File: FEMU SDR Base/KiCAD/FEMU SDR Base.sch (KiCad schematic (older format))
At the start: 93 parts, among them M1 M1, M10 M1, M11 M1, M12 M1, M13 M1, M14 M1, M15 M1, M16 M1, M17 SMA1, M18 SMA2, M2 M1, M3 M1, M4 M1, M5 M1, M6 M1, M7 M1, M8 M1, M9 M1, P1 Battery, P10 PWM2, P11 PWM3, P12 PWM4, P13 PWM1, P14 PWM2, P15 PWM3, P16 PWM4, P17 12V, P18 GND, P19 12V, P2 SDR_Shield_1, P20 GND, P21 SDR0, P22 SDR1, P27 PWM0, P28 PWM5, P29 PWM6, P3 SDR_Shield_2, P30 PWM7, P31 PWM0, P32 PWM5, P33 PWM6, P34 PWM7, P35 Battery, P36 RPi, P37 PXH, P38 Rx, P4 12V, P5 GND, P6 12V, P7 GND, P8 Raspi_Power_Shield, P9 PWM1, U1 TPS562209, U2 LP38858-LDO, U3 LP38858-LDO, U4 LM1117, U5 LM1117

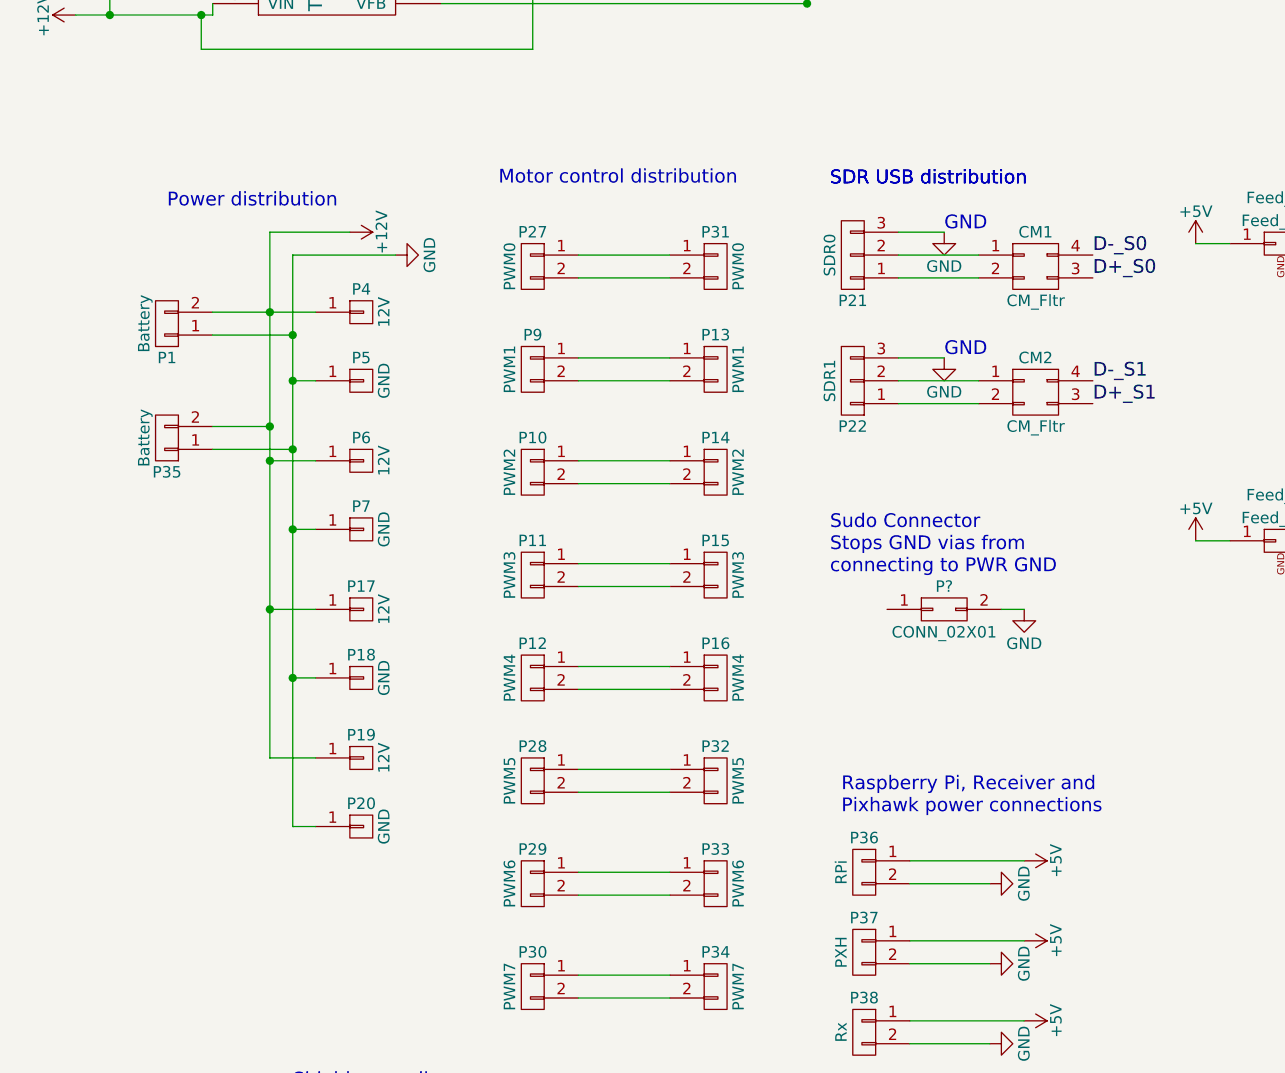
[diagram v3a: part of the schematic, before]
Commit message: Disconnected VIA connections from GND (layer2) onto PWR_GND current zones for motor return. Added sudo pads in Schematic to allow the GND and PWR_GND nets to connect
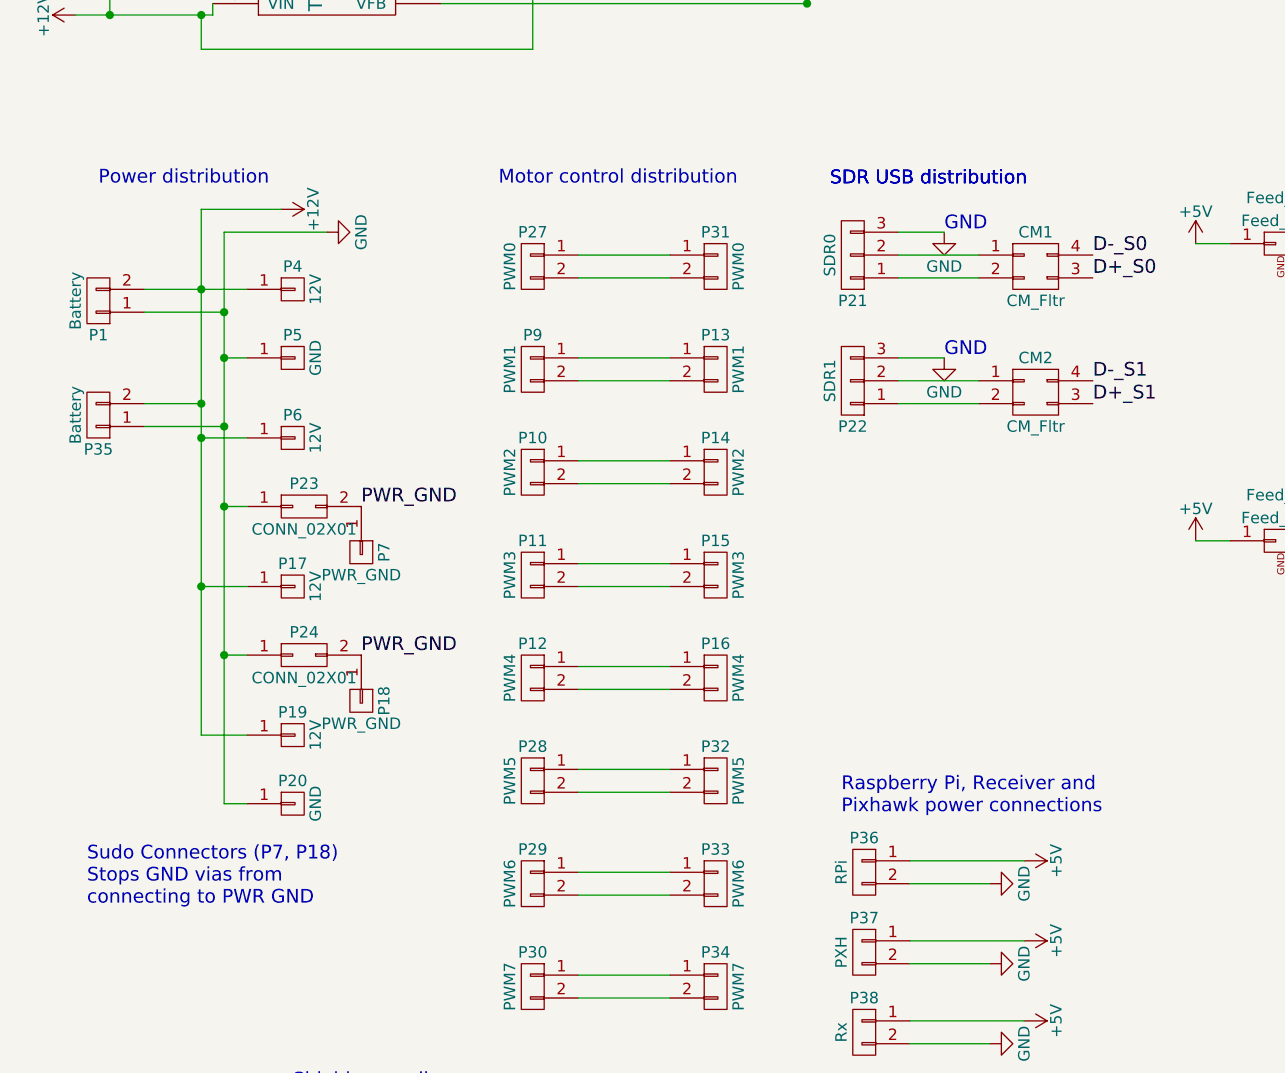
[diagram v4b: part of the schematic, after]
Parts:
- added P24: CONN_02X01, ARB_foots:Conn_PWR_GND_to_GND, symbol CONN_02X01
- C23: footprint Capacitors_SMD:C_0805_HandSoldering -> Capacitors_SMD:C_0603_HandSoldering
- P18, P7: value GND -> PWR_GND
- P23: renamed from P?; footprint (none) -> ARB_foots:Conn_PWR_GND_to_GND
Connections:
- net GND: now also P23.1 (P1), P24.1 (P1); no longer P18.1 (P1), P23.2 (P2), P7.1 (P1)
- new net PWR_GND: P18.1 (P1), P23.2 (P2), P24.2 (P2), P7.1 (P1)
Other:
- note added: "Sudo Connectors (P7, P18)\nStops GND vias from \nconnecting to PWR GND"
- note removed: "Sudo Connector\nStops GND vias from \nconnecting to PWR GND"
- moved on the sheet: P1, P17, P18, P19, P20, P23, P35, P4, P5, P6, P7
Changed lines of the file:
@@
 L CONN_01X02 P1
 U 1 1 572239A5
-P 1100 2950
-F 0 "P1" H 1100 3100 50  0000 C CNN
-F 1 "Battery" V 1200 2950 50  0000 C CNN
-F 2 "Misc footprints:XT60" H 1100 2950 50  0001 C CNN
-F 3 "" H 1100 2950 50  0000 C CNN
-	1    1100 2950
+P 800 2850
+F 0 "P1" H 800 3000 50  0000 C CNN
+F 1 "Battery" V 900 2850 50  0000 C CNN
+F 2 "Misc footprints:XT60" H 800 2850 50  0001 C CNN
+F 3 "" H 800 2850 50  0000 C CNN
+	1    800  2850
 	-1   0    0    1
 $EndComp
@@
 L +12V #PWR03
 U 1 1 5722422D
-P 1900 2550
-F 0 "#PWR03" H 1900 2400 50  0001 C CNN
-F 1 "+12V" H 1900 2690 50  0000 C CNN
-F 2 "" H 1900 2550 50  0000 C CNN
-F 3 "" H 1900 2550 50  0000 C CNN
-	1    1900 2550
+P 1600 2450
+F 0 "#PWR03" H 1600 2300 50  0001 C CNN
+F 1 "+12V" H 1600 2590 50  0000 C CNN
+F 2 "" H 1600 2450 50  0000 C CNN
+F 3 "" H 1600 2450 50  0000 C CNN
+	1    1600 2450
 	0    1    1    0
 $EndComp
-Text Notes 1100 2450 0    60   ~ 0
+Text Notes 800  2350 0    60   ~ 0
 Power distribution\n
 $Comp
@@
 L CONN_01X01 P4
 U 1 1 57343B65
-P 1950 2900
-F 0 "P4" H 1950 3000 50  0000 C CNN
-F 1 "12V" V 2050 2900 50  0000 C CNN
-F 2 "SMD_Packages:1Pin" H 1950 2900 50  0001 C CNN
-F 3 "" H 1950 2900 50  0000 C CNN
-	1    1950 2900
+P 1650 2800
+F 0 "P4" H 1650 2900 50  0000 C CNN
+F 1 "12V" V 1750 2800 50  0000 C CNN
+F 2 "SMD_Packages:1Pin" H 1650 2800 50  0001 C CNN
+F 3 "" H 1650 2800 50  0000 C CNN
+	1    1650 2800
 	1    0    0    -1
 $EndComp
@@
 L CONN_01X01 P5
 U 1 1 57343E6C
-P 1950 3200
-F 0 "P5" H 1950 3300 50  0000 C CNN
-F 1 "GND" V 2050 3200 50  0000 C CNN
-F 2 "SMD_Packages:1Pin" H 1950 3200 50  0001 C CNN
-F 3 "" H 1950 3200 50  0000 C CNN
-	1    1950 3200
+P 1650 3100
+F 0 "P5" H 1650 3200 50  0000 C CNN
+F 1 "GND" V 1750 3100 50  0000 C CNN
+F 2 "SMD_Packages:1Pin" H 1650 3100 50  0001 C CNN
+F 3 "" H 1650 3100 50  0000 C CNN
+	1    1650 3100
 	1    0    0    -1
 $EndComp
@@
 L CONN_01X01 P6
 U 1 1 57344192
-P 1950 3550
-F 0 "P6" H 1950 3650 50  0000 C CNN
-F 1 "12V" V 2050 3550 50  0000 C CNN
-F 2 "SMD_Packages:1Pin" H 1950 3550 50  0001 C CNN
-F 3 "" H 1950 3550 50  0000 C CNN
-	1    1950 3550
+P 1650 3450
+F 0 "P6" H 1650 3550 50  0000 C CNN
+F 1 "12V" V 1750 3450 50  0000 C CNN
+F 2 "SMD_Packages:1Pin" H 1650 3450 50  0001 C CNN
+F 3 "" H 1650 3450 50  0000 C CNN
+	1    1650 3450
 	1    0    0    -1
 $EndComp
@@
 L CONN_01X01 P7
 U 1 1 57344242
-P 1950 3850
-F 0 "P7" H 1950 3950 50  0000 C CNN
-F 1 "GND" V 2050 3850 50  0000 C CNN
-F 2 "SMD_Packages:1Pin" H 1950 3850 50  0001 C CNN
-F 3 "" H 1950 3850 50  0000 C CNN
-	1    1950 3850
-	1    0    0    -1
+P 1950 3950
+F 0 "P7" H 1950 4050 50  0000 C CNN
+F 1 "PWR_GND" V 2050 3950 50  0000 C CNN
+F 2 "SMD_Packages:1Pin" H 1950 3950 50  0001 C CNN
+F 3 "" H 1950 3950 50  0000 C CNN
+	1    1950 3950
+	0    1    1    0
 $EndComp
 $Comp
 L CONN_01X01 P17
 U 1 1 57345117
-P 1950 4200
-F 0 "P17" H 1950 4300 50  0000 C CNN
-F 1 "12V" V 2050 4200 50  0000 C CNN
-F 2 "SMD_Packages:1Pin" H 1950 4200 50  0001 C CNN
-F 3 "" H 1950 4200 50  0000 C CNN
-	1    1950 4200
+P 1650 4100
+F 0 "P17" H 1650 4200 50  0000 C CNN
+F 1 "12V" V 1750 4100 50  0000 C CNN
+F 2 "SMD_Packages:1Pin" H 1650 4100 50  0001 C CNN
+F 3 "" H 1650 4100 50  0000 C CNN
+	1    1650 4100
 	1    0    0    -1
 $EndComp
@@
 L CONN_01X01 P18
 U 1 1 5734511D
-P 1950 4500
-F 0 "P18" H 1950 4600 50  0000 C CNN
-F 1 "GND" V 2050 4500 50  0000 C CNN
-F 2 "SMD_Packages:1Pin" H 1950 4500 50  0001 C CNN
-F 3 "" H 1950 4500 50  0000 C CNN
-	1    1950 4500
-	1    0    0    -1
+P 1950 4600
+F 0 "P18" H 1950 4700 50  0000 C CNN
+F 1 "PWR_GND" V 2050 4600 50  0000 C CNN
+F 2 "SMD_Packages:1Pin" H 1950 4600 50  0001 C CNN
+F 3 "" H 1950 4600 50  0000 C CNN
+	1    1950 4600
+	0    1    1    0
 $EndComp
 $Comp
 L CONN_01X01 P19
 U 1 1 5734526F
-P 1950 4850
-F 0 "P19" H 1950 4950 50  0000 C CNN
-F 1 "12V" V 2050 4850 50  0000 C CNN
-F 2 "SMD_Packages:1Pin" H 1950 4850 50  0001 C CNN
-F 3 "" H 1950 4850 50  0000 C CNN
-	1    1950 4850
+P 1650 4750
+F 0 "P19" H 1650 4850 50  0000 C CNN
+F 1 "12V" V 1750 4750 50  0000 C CNN
+F 2 "SMD_Packages:1Pin" H 1650 4750 50  0001 C CNN
+F 3 "" H 1650 4750 50  0000 C CNN
+	1    1650 4750
 	1    0    0    -1
 $EndComp
@@
 L CONN_01X01 P20
 U 1 1 57345275
-P 1950 5150
-F 0 "P20" H 1950 5250 50  0000 C CNN
-F 1 "GND" V 2050 5150 50  0000 C CNN
-F 2 "SMD_Packages:1Pin" H 1950 5150 50  0001 C CNN
-F 3 "" H 1950 5150 50  0000 C CNN
-	1    1950 5150
+P 1650 5050
+F 0 "P20" H 1650 5150 50  0000 C CNN
+F 1 "GND" V 1750 5050 50  0000 C CNN
+F 2 "SMD_Packages:1Pin" H 1650 5050 50  0001 C CNN
+F 3 "" H 1650 5050 50  0000 C CNN
+	1    1650 5050
 	1    0    0    -1
 $EndComp
@@
 L GND #PWR015
 U 1 1 5734BB86
-P 2100 2650
-F 0 "#PWR015" H 2100 2400 50  0001 C CNN
-F 1 "GND" H 2100 2500 50  0000 C CNN
-F 2 "" H 2100 2650 50  0000 C CNN
-F 3 "" H 2100 2650 50  0000 C CNN
-	1    2100 2650
+P 1800 2550
+F 0 "#PWR015" H 1800 2300 50  0001 C CNN
+F 1 "GND" H 1800 2400 50  0000 C CNN
+F 2 "" H 1800 2550 50  0000 C CNN
+F 3 "" H 1800 2550 50  0000 C CNN
+	1    1800 2550
 	0    -1   -1   0
 $EndComp
@@
 F 0 "C23" H 8475 4550 50  0000 L CNN
 F 1 "10uF" H 8475 4350 50  0000 L CNN
-F 2 "Capacitors_SMD:C_0805_HandSoldering" H 8488 4300 50  0001 C CNN
+F 2 "Capacitors_SMD:C_0603_HandSoldering" H 8488 4300 50  0001 C CNN
 F 3 "" H 8450 4450 50  0000 C CNN
 	1    8450 4450
@@
 	3350 1100 3150 1100
 Wire Wire Line
-	1550 2550 1900 2550
+	1250 2450 1600 2450
 Wire Wire Line
 	2900 3100 3300 3100
@@
 	10350 4250 10350 4100
 Wire Wire Line
-	1300 2900 1750 2900
-Wire Wire Line
-	1550 2550 1550 4850
-Connection ~ 1550 2900
-Wire Wire Line
-	1650 2650 1650 5150
-Wire Wire Line
-	1650 3200 1750 3200
-Wire Wire Line
-	1650 2650 2100 2650
-Connection ~ 1650 3000
+	1000 2800 1450 2800
+Wire Wire Line
+	1250 2450 1250 4750
+Connection ~ 1250 2800
+Wire Wire Line
+	1350 2550 1350 5050
+Wire Wire Line
+	1350 3100 1450 3100
+Wire Wire Line
+	1350 2550 1800 2550
+Connection ~ 1350 2900
 Connection ~ 3350 1350
 Wire Wire Line
-	1650 3850 1750 3850
-Connection ~ 1650 3200
-Wire Wire Line
-	1650 4500 1750 4500
-Connection ~ 1650 3850
-Wire Wire Line
-	1650 5150 1750 5150
-Connection ~ 1650 4500
-Wire Wire Line
-	1550 3550 1750 3550
-Wire Wire Line
-	1550 4200 1750 4200
-Connection ~ 1550 3550
-Wire Wire Line
-	1550 4850 1750 4850
-Connection ~ 1550 4200
+	1350 3750 1450 3750
+Connection ~ 1350 3100
+Wire Wire Line
+	1350 4400 1450 4400
+Connection ~ 1350 3750
+Wire Wire Line
+	1350 5050 1450 5050
+Connection ~ 1350 4400
+Wire Wire Line
+	1250 3450 1450 3450
+Wire Wire Line
+	1250 4100 1450 4100
+Connection ~ 1250 3450
+Wire Wire Line
+	1250 4750 1450 4750
+Connection ~ 1250 4100
 Wire Wire Line
 	2900 4900 3300 4900
@@
 L CONN_01X02 P35
 U 1 1 5736ACD2
-P 1100 3450
-F 0 "P35" H 1100 3600 50  0000 C CNN
-F 1 "Battery" V 1200 3450 50  0000 C CNN
-F 2 "Misc footprints:XT60" H 1100 3450 50  0001 C CNN
-F 3 "" H 1100 3450 50  0000 C CNN
-	1    1100 3450
+P 800 3350
+F 0 "P35" H 800 3500 50  0000 C CNN
+F 1 "Battery" V 900 3350 50  0000 C CNN
+F 2 "Misc footprints:XT60" H 800 3350 50  0001 C CNN
+F 3 "" H 800 3350 50  0000 C CNN
+	1    800  3350
 	-1   0    0    1
 $EndComp
 Wire Wire Line
-	1300 3400 1550 3400
-Connection ~ 1550 3400
-Wire Wire Line
-	1300 3500 1650 3500
-Connection ~ 1650 3500
-Wire Wire Line
-	1300 3000 1650 3000
+	1000 3300 1250 3300
+Connection ~ 1250 3300
+Wire Wire Line
+	1000 3400 1350 3400
+Connection ~ 1350 3400
+Wire Wire Line
+	1000 2900 1350 2900
 Text Notes 4250 6500 0    60   ~ 0
 Grounded mounting rings\n\n
@@
 	1    0    0    -1
 $EndComp
-$Comp
-L CONN_02X01 P?
+Text Notes 750  5500 0    60   ~ 0
+Sudo Connectors (P7, P18)\nStops GND vias from \nconnecting to PWR GND
+Text Label 1950 4400 0    60   ~ 0
+PWR_GND
+Text Label 1950 3750 0    60   ~ 0
+PWR_GND
+$Comp
+L CONN_02X01 P24
+U 1 1 573F719D
+P 1700 4400
+F 0 "P24" H 1700 4500 50  0000 C CNN
+F 1 "CONN_02X01" H 1700 4300 50  0000 C CNN
+F 2 "ARB_foots:Conn_PWR_GND_to_GND" H 1700 3200 50  0001 C CNN
+F 3 "" H 1700 3200 50  0000 C CNN
+	1    1700 4400
+	1    0    0    -1
+$EndComp
+$Comp
+L CONN_02X01 P23
 U 1 1 573F1A94
-P 4500 4200
-F 0 "P?" H 4500 4300 50  0000 C CNN
-F 1 "CONN_02X01" H 4500 4100 50  0000 C CNN
-F 2 "" H 4500 3000 50  0000 C CNN
-F 3 "" H 4500 3000 50  0000 C CNN
-	1    4500 4200
-	1    0    0    -1
-$EndComp
-Text Notes 4000 4050 0    60   ~ 0
-Sudo Connector\nStops GND vias from \nconnecting to PWR GND
-$Comp
-L GND #PWR?
-U 1 1 573F2142
-P 4850 4200
-F 0 "#PWR?" H 4850 3950 50  0001 C CNN
-F 1 "GND" H 4850 4050 50  0000 C CNN
-F 2 "" H 4850 4200 50  0000 C CNN
-F 3 "" H 4850 4200 50  0000 C CNN
-	1    4850 4200
-	1    0    0    -1
-$EndComp
-Wire Wire Line
-	4850 4200 4750 4200
+P 1700 3750
+F 0 "P23" H 1700 3850 50  0000 C CNN
+F 1 "CONN_02X01" H 1700 3650 50  0000 C CNN
+F 2 "ARB_foots:Conn_PWR_GND_to_GND" H 1700 2550 50  0001 C CNN
+F 3 "" H 1700 2550 50  0000 C CNN
+	1    1700 3750
+	1    0    0    -1
+$EndComp
 $EndSCHEMATC
